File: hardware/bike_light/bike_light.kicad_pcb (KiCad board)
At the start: 2 copper layers, 65 x 22 mm, 48 parts, among them J1 Battery, J2 USB_C_Receptacle_USB2.0_16P, SW1 SW_Push, SW2 SW_Push, U1 TPS22918DBV, U2 ESP32-C3-WROOM-02, U3 XC6220B331MR, U4 BQ21040DBV

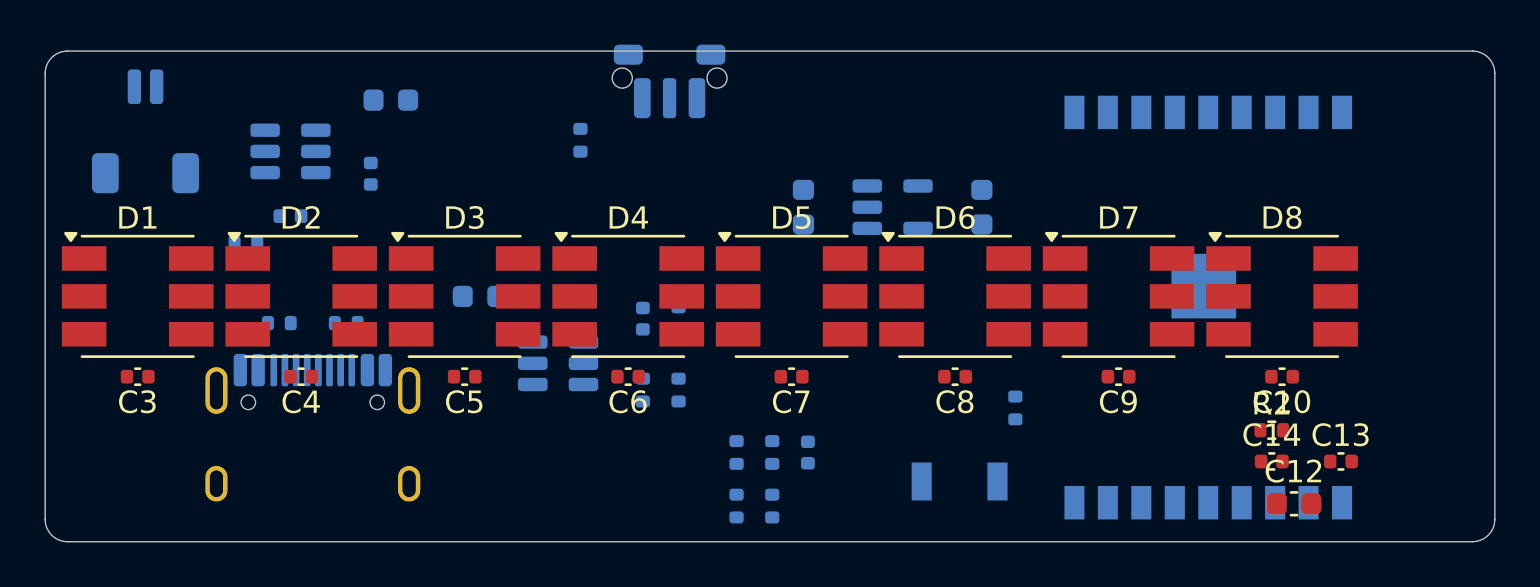
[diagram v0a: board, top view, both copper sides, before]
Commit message: PCB updates
* Added USB step file
* Added side push button step file
* Moved debug pads for cleaner layout
* Added some silkscreening with model name/version.
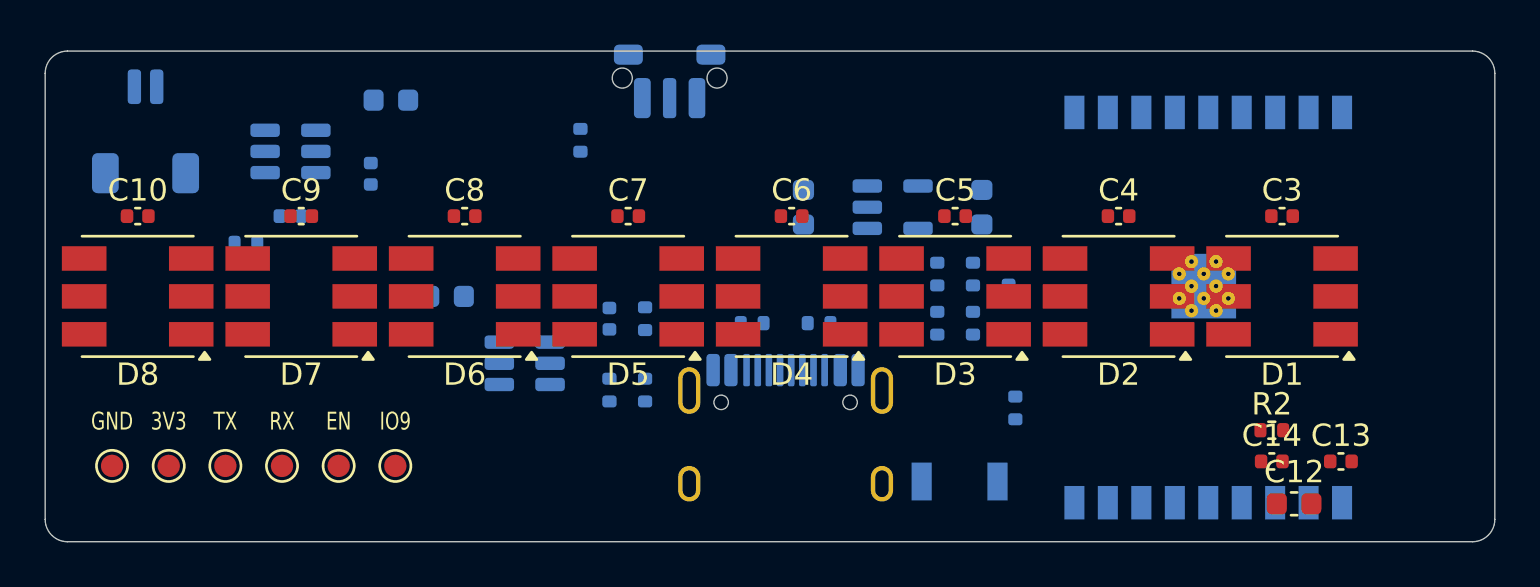
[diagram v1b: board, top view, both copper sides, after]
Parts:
- added TP1: 3V3, TestPoint:TestPoint_Pad_D1.0mm, F.Cu at (105.5, 118.6)
- added TP2: EN, TestPoint:TestPoint_Pad_D1.0mm, F.Cu at (113.2, 118.6)
- added TP3: IO9_BOOT, TestPoint:TestPoint_Pad_D1.0mm, F.Cu at (115.7, 118.6)
- added TP4: TXD, TestPoint:TestPoint_Pad_D1.0mm, F.Cu at (108.1, 118.6)
- added TP5: RXD, TestPoint:TestPoint_Pad_D1.0mm, F.Cu at (110.6, 118.6)
- added TP6: GND, TestPoint:TestPoint_Pad_D1.0mm, F.Cu at (103.0, 118.6)
- J2: footprint Connector_USB:USB_C_Receptacle_HRO_TYPE-C-31-M-12 -> bike_light:USB_C_Receptacle_HRO_TYPE-C-31-M-12
- SW1: footprint Button_Switch_SMD:SW_Push_1P1T-MP_NO_Horizontal_Alps_SKRTLAE010 -> bike_light:SW_Push_1P1T-MP_NO_Horizontal_Alps_SKRTLAE010
- U2: footprint bike_light:ESP32-C3-WROOM-02_NoVias -> RF_Module:ESP32-C3-WROOM-02
- moved C10 51.8 mm to (104.2, 107.4), turned to 0 degrees
- moved C3 51.8 mm to (155.5, 107.4), turned to 0 degrees
- moved D1 51.3 mm to (155.5, 111.0), turned to 180 degrees
- moved D8 51.3 mm to (104.2, 111.0), turned to 180 degrees
- moved C4 37.4 mm to (148.1, 107.4), turned to 0 degrees
- moved C9 37.4 mm to (111.5, 107.4), turned to 0 degrees
- moved D2 36.6 mm to (148.1, 111.0), turned to 180 degrees
- moved D7 36.6 mm to (111.5, 111.0), turned to 180 degrees
- moved C5 23.1 mm to (140.8, 107.4), turned to 0 degrees
- moved C8 23.1 mm to (118.8, 107.4), turned to 0 degrees
- moved D3 22.0 mm to (140.8, 111.0), turned to 180 degrees
- moved D6 22.0 mm to (118.8, 111.0), turned to 180 degrees
- moved J2 21.2 mm to (133.2, 118.3)
- moved R5 21.2 mm to (131.7, 112.2)
- moved R6 21.2 mm to (134.7, 112.2)
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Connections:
- net Net-(U2-IO9) renamed /BOOT
- U2 pad 11: unconnected-(U2-IO20/RXD-Pad11) -> /UART_RX
- U2 pad 12: unconnected-(U2-IO21/TXD-Pad12) -> /UART_TX
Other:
- board text added: "+"
- board text added: "-"
- board text added: "3V3"
- board text added: "BOOT"
- board text added: "EN"
- board text added: "GND"
- board text added: "IO9"
- board text added: "MODE"
- board text added: "RX"
- board text added: "TX"
- board text added: "gladish_bl rev0.0.1"

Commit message: Updated PCB and new models
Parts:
- U2: footprint RF_Module:ESP32-C3-WROOM-02 -> bike_light:ESP32-C3-WROOM-02_NoVias
- moved SW1 0.35 mm to (128.0, 101.6)
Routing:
- added copper zone on B.Cu, net GND
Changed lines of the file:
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@@
 	)
 	(paper "A4")
+	(title_block
+		(title "gladish_bl")
+		(date "2026-10-16")
+		(rev "0.0.1")
+	)
 	(layers
 		(0 "F.Cu" signal)
@@
 		)
 	)
-	(footprint "RF_Module:ESP32-C3-WROOM-02"
+	(footprint "bike_light:ESP32-C3-WROOM-02_NoVias"
 		(layer "B.Cu")
 		(at 152.15 111.5 90)
-		(descr "RF Module, ESP32-C3 WROOM-02, Wi-Fi and Bluetooth, BLE, onboard antenna, https://www.espressif.com/sites/default/files/documentation/esp32-c3-wroom-02_datasheet_en.pdf")
+		(descr "RF Module, ESP32-C3 WROOM-02, Wi-Fi and Bluetooth, BLE, onboard antenna, https://www.espressif.com/sites/default/files/documentation/esp32-c3-wroom-02_datasheet_en.pdf; thermal vias under ground pad removed so front-side parts can sit over it")
 		(tags "ESP32-C3 WROOM-02 espressif")
 		(property "Reference" "U2"
@@
 			(pintype "bidirectional+no_connect")
 		)
-		(pad "19" thru_hole circle
-			(at -0.14 -0.75 90)
-			(size 0.6 0.6)
-			(drill 0.2)
-			(property pad_prop_heatsink)
-			(layers "*.Cu" "B.Mask")
-			(remove_unused_layers no)
-			(net "GND")
-			(pinfunction "GND_19")
-			(pintype "passive")
-			(zone_connect 2)
-		)
-		(pad "19" thru_hole circle
-			(at -0.14 0.35 90)
-			(size 0.6 0.6)
-			(drill 0.2)
-			(property pad_prop_heatsink)
-			(layers "*.Cu" "B.Mask")
-			(remove_unused_layers no)
-			(net "GND")
-			(pinfunction "GND_19")
-			(pintype "passive")
-			(zone_connect 2)
-		)
-		(pad "19" thru_hole circle
-			(at 0.41 -1.3 90)
-			(size 0.6 0.6)
-			(drill 0.2)
-			(property pad_prop_heatsink)
-			(layers "*.Cu" "B.Mask")
-			(remove_unused_layers no)
-			(net "GND")
-			(pinfunction "GND_19")
-			(pintype "passive")
-			(zone_connect 2)
-		)
-		(pad "19" thru_hole circle
-			(at 0.41 -0.2 90)
-			(size 0.6 0.6)
-			(drill 0.2)
-			(property pad_prop_heatsink)
-			(layers "*.Cu" "B.Mask")
-			(remove_unused_layers no)
-			(net "GND")
-			(pinfunction "GND_19")
-			(pintype "passive")
-			(zone_connect 2)
-		)
-		(pad "19" thru_hole circle
-			(at 0.41 0.9 90)
-			(size 0.6 0.6)
-			(drill 0.2)
-			(property pad_prop_heatsink)
-			(layers "*.Cu" "B.Mask")
-			(remove_unused_layers no)
-			(net "GND")
-			(pinfunction "GND_19")
-			(pintype "passive")
-			(zone_connect 2)
-		)
-		(pad "19" thru_hole circle
-			(at 0.96 -0.75 90)
-			(size 0.6 0.6)
-			(drill 0.2)
-			(property pad_prop_heatsink)
-			(layers "*.Cu" "B.Mask")
-			(remove_unused_layers no)
-			(net "GND")
-			(pinfunction "GND_19")
-			(pintype "passive")
-			(zone_connect 2)
-		)
 		(pad "19" smd rect
 			(at 0.96 -0.2 90)
@@
 			(zone_connect 2)
 		)
-		(pad "19" thru_hole circle
-			(at 0.96 0.35 90)
-			(size 0.6 0.6)
-			(drill 0.2)
-			(property pad_prop_heatsink)
-			(layers "*.Cu" "B.Mask")
-			(remove_unused_layers no)
-			(net "GND")
-			(pinfunction "GND_19")
-			(pintype "passive")
-			(zone_connect 2)
-		)
-		(pad "19" thru_hole circle
-			(at 1.51 -1.3 90)
-			(size 0.6 0.6)
-			(drill 0.2)
-			(property pad_prop_heatsink)
-			(layers "*.Cu" "B.Mask")
-			(remove_unused_layers no)
-			(net "GND")
-			(pinfunction "GND_19")
-			(pintype "passive")
-			(zone_connect 2)
-		)
-		(pad "19" thru_hole circle
-			(at 1.51 -0.2 90)
-			(size 0.6 0.6)
-			(drill 0.2)
-			(property pad_prop_heatsink)
-			(layers "*.Cu" "B.Mask")
-			(remove_unused_layers no)
-			(net "GND")
-			(pinfunction "GND_19")
-			(pintype "passive")
-			(zone_connect 2)
-		)
-		(pad "19" thru_hole circle
-			(at 1.51 0.9 90)
-			(size 0.6 0.6)
-			(drill 0.2)
-			(property pad_prop_heatsink)
-			(layers "*.Cu" "B.Mask")
-			(remove_unused_layers no)
-			(net "GND")
-			(pinfunction "GND_19")
-			(pintype "passive")
-			(zone_connect 2)
-		)
-		(pad "19" thru_hole circle
-			(at 2.06 -0.75 90)
-			(size 0.6 0.6)
-			(drill 0.2)
-			(property pad_prop_heatsink)
-			(layers "*.Cu" "B.Mask")
-			(remove_unused_layers no)
-			(net "GND")
-			(pinfunction "GND_19")
-			(pintype "passive")
-			(zone_connect 2)
-		)
-		(pad "19" thru_hole circle
-			(at 2.06 0.35 90)
-			(size 0.6 0.6)
-			(drill 0.2)
-			(property pad_prop_heatsink)
-			(layers "*.Cu" "B.Mask")
-			(remove_unused_layers no)
-			(net "GND")
-			(pinfunction "GND_19")
-			(pintype "passive")
-			(zone_connect 2)
-		)
 		(zone
 			(layers "F.Cu" "B.Cu")
@@
 			(pinfunction "GND_A1")
 			(pintype "passive")
+			(zone_connect 2)
 		)
 		(pad "A4" smd roundrect
@@
 			(pinfunction "GND_A12")
 			(pintype "passive")
+			(zone_connect 2)
 		)
 		(pad "B1" smd roundrect
@@
 			(pinfunction "GND_B1")
 			(pintype "passive")
+			(zone_connect 2)
 		)
 		(pad "B4" smd roundrect
@@
 			(pinfunction "GND_B12")
 			(pintype "passive")
+			(zone_connect 2)
 		)
 		(pad "SH" thru_hole oval
@@
 	(footprint "bike_light:SW_Push_1P1T-MP_NO_Horizontal_Alps_SKRTLAE010"
 		(layer "B.Cu")
-		(at 128 101.21)
+		(at 128 101.56)
 		(descr "Side push button (https://www.alps.com/prod/info/E/PDF/Tact/SurfaceMount/SKRT/SKRT.pdf)")
 		(tags "push horizontal SPST 1P1T")
@@
 	)
 	(gr_text "-"
-		(at 102 101.7 0)
+		(at 101.3 101.7 0)
 		(layer "B.SilkS")
 		(effects
@@
 	)
 	(gr_text "+"
-		(at 107 101.7 0)
+		(at 107.7 101.7 0)
 		(layer "B.SilkS")
 		(effects
@@
 	)
 	(gr_text "MODE"
-		(at 128 104.6 0)
+		(at 128 105.5 0)
 		(layer "B.SilkS")
 		(effects
@@
 		)
 	)
+	(zone
+		(net "GND")
+		(layer "B.Cu")
+		(name "GND_B")
+		(hatch edge 0.5)
+		(connect_pads
+			(clearance 0.2)
+		)
+		(min_thickness 0.2)
+		(fill yes
+			(thermal_gap 0.3)
+			(thermal_bridge_width 0.3)
+			(island_removal_mode 0)
+		)
+		(polygon
+			(pts
+				(xy 100 100) (xy 165 100) (xy 165 122) (xy 100 122)
+			)
+		)
+	)

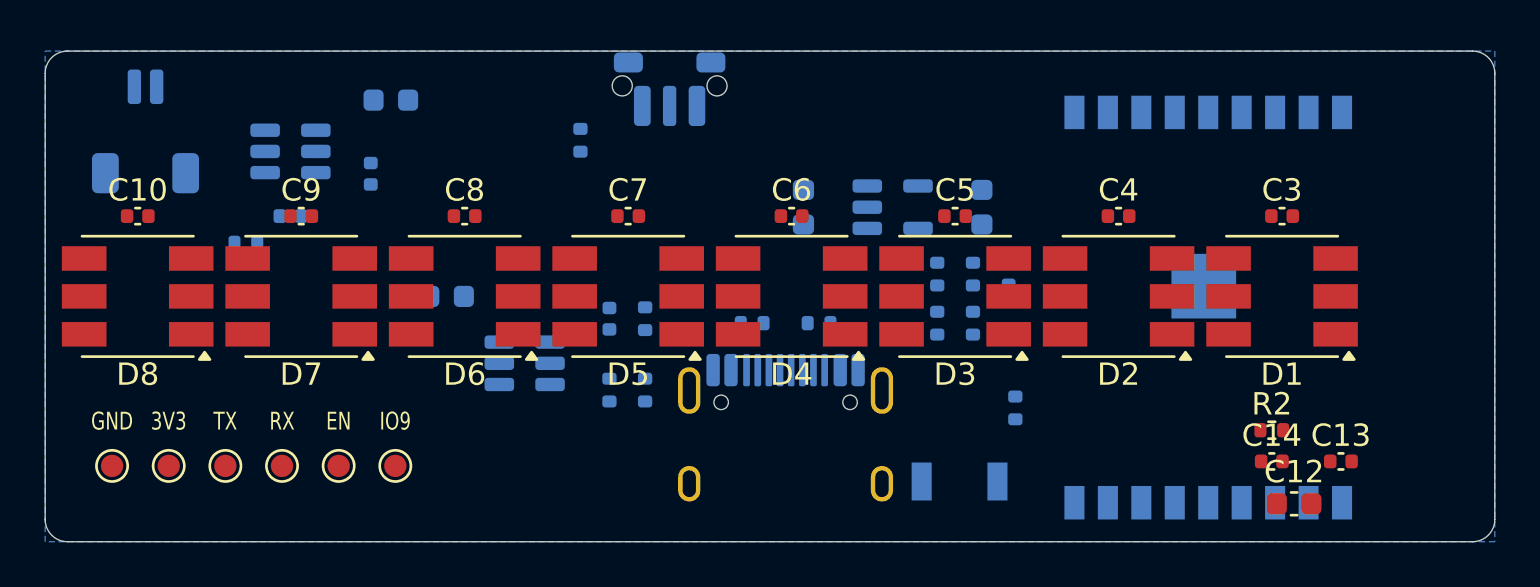
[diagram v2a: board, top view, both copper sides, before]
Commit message: First run of autorouting complete
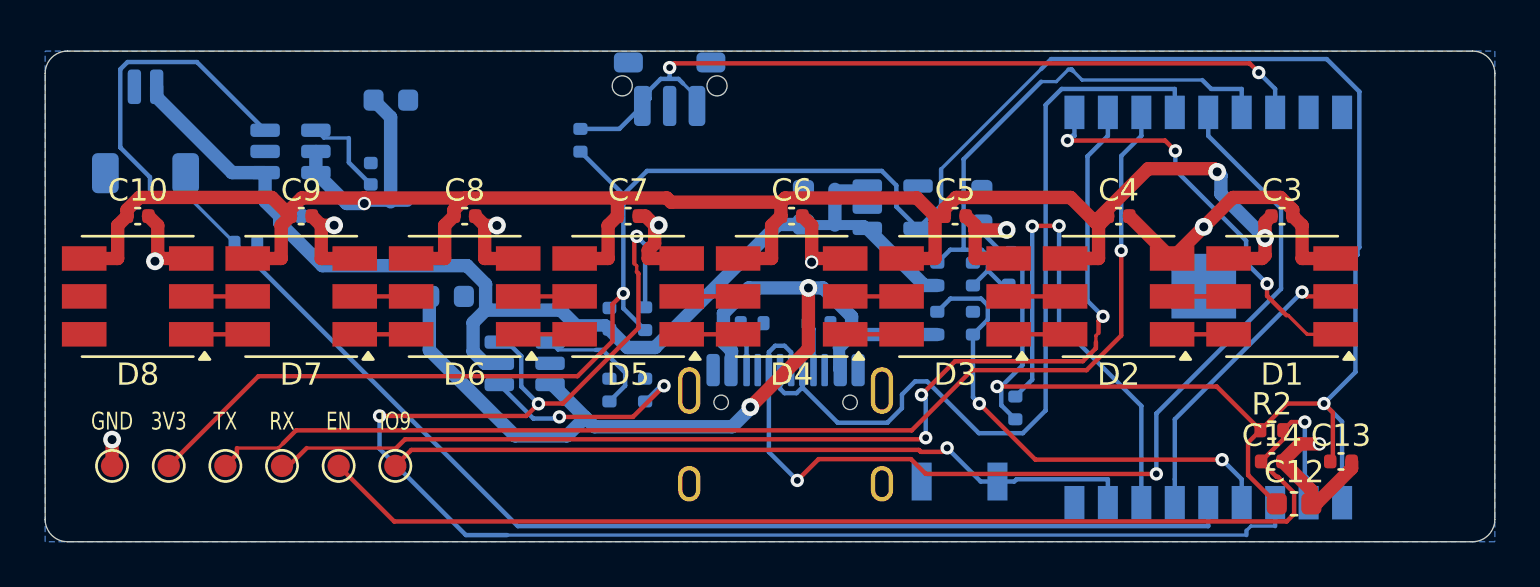
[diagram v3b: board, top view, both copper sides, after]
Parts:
- moved R5 3.00 mm to (134.7, 112.2)
- moved R6 3.00 mm to (131.7, 112.2)
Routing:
- net +3.3V: track 0.00 -> 126.6 mm, vias 0 -> 3
- net /LED_VDD: track 0.00 -> 98.5 mm, vias 0 -> 3
- net /CHG_STAT: track 0.00 -> 69.1 mm, vias 0 -> 3
- net /LED_EN: track 0.00 -> 68.9 mm
- net /ESP_EN: track 0.00 -> 53.6 mm, vias 0 -> 1
- net /UART_TX: track 0.00 -> 53.1 mm, vias 0 -> 1
- net +BATT: track 0.00 -> 51.8 mm
- net /UART_RX: track 0.00 -> 51.4 mm, vias 0 -> 3
- net GND: track 0.00 -> 46.6 mm, vias 0 -> 9
- net /USB_D+: track 0.00 -> 45.0 mm, vias 0 -> 2
- net VBUS: track 0.00 -> 43.9 mm, vias 0 -> 2
- net /USB_D-: track 0.00 -> 37.7 mm
- net /BUTTON: track 0.00 -> 36.4 mm, vias 0 -> 2
- net /BOOT: track 0.00 -> 34.1 mm, vias 0 -> 1
- net /VBAT_SENSE: track 0.00 -> 25.0 mm
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
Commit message: Fixed a bunch of DRC problems
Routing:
- net GND: track 46.6 -> 86.8 mm, vias 9 -> 36
- net /LED_VDD: track 98.5 -> 97.7 mm
- net +3.3V: track 126.6 -> 126.0 mm
